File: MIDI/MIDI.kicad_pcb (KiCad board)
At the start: 2 copper layers, 85.8 x 137 mm, 136 parts, among them J1 DIN_5, J2 DIN_5, J3 DIN_5, J4 CONN_01X06, J5 CONN_01X06, SW1 SW_PUSH, SW10 SW_PUSH, SW11 SW_PUSH, SW12 SW_PUSH, SW2 SW_PUSH, SW3 SW_PUSH, SW4 SW_PUSH, SW5 SW_PUSH, SW6 SW_PUSH, SW7 SW_PUSH, SW8 SW_PUSH, SW9 SW_PUSH, U1 6N138, U2 4050, U3 40106, U4 ENCODER_w_SWITCH, U5 ENCODER_w_SWITCH, U6 ENCODER_w_SWITCH

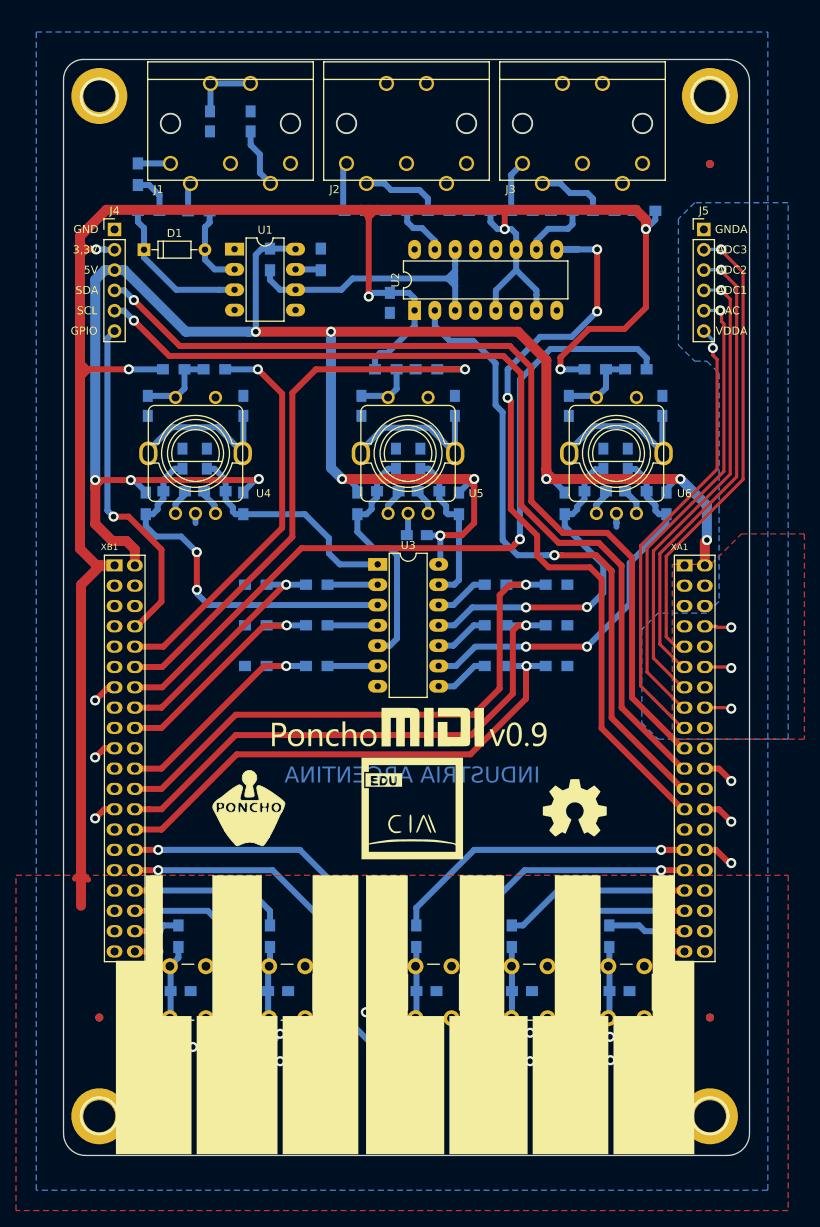
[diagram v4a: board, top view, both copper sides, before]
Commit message: Se finalizan los cambios según las revisiones
> Se realizan cambios segun detalles en archivos de revisiones.
> Se abandona requisito para asegurar fabricación artesanal por lo que se comienzan a utilizar los orificios metalizados para rutear.
> Se cambia la tensión de fijación de las compuertas no utilizadas en el 4050 para mejorar el plano de masa debajo del mismo.
> Se genera la versión 1.0 del diseño.
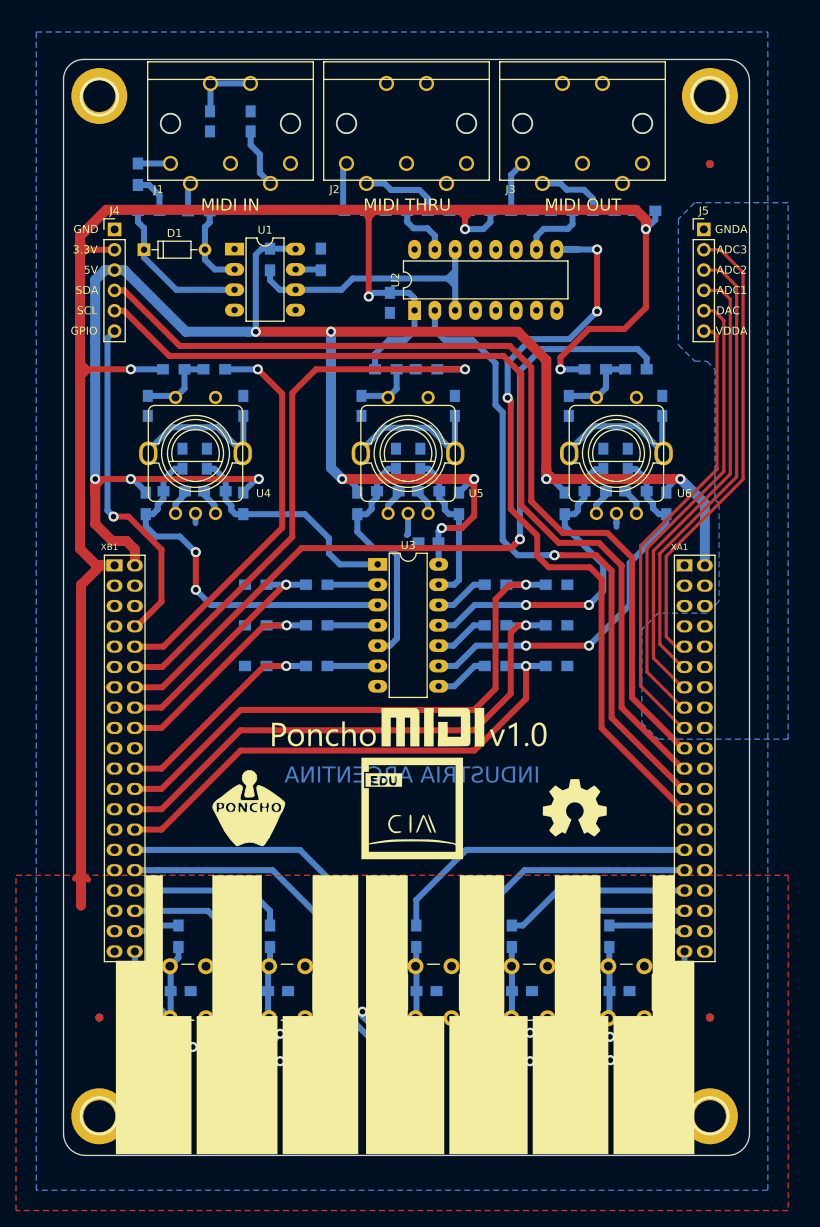
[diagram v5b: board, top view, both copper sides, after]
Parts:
- moved C16 1.72 mm to (87.1, 86.1)
- moved R39 0.51 mm to (52.1, 145.3)
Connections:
- U2 pad 11: +3.3V -> GND
- U2 pad 5: +3.3V -> GND
- U2 pad 7: +3.3V -> GND
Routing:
- net GND: track 26.2 -> 7.13 mm, vias 6 -> 0
- net +3.3V: track 318.9 -> 306.9 mm, vias 14 -> 13
- net GNDA: track 10.1 -> 0.00 mm, vias 3 -> 0
- net /Conectores/PUL0: track 21.1 -> 14.6 mm, vias 1 -> 0
- net /Conectores/PUL11: track 17.9 -> 14.7 mm, vias 1 -> 0
- net +5V: track 252.7 -> 251.1 mm, vias 11 -> 10
- net /Conectores/ENC_SW2: track 95.1 -> 95.7 mm
- net /Conectores/VDDA: track 56.7 -> 57.3 mm, vias 1 -> 0
- net /Conectores/PUL6: track 38.7 -> 39.3 mm, vias 1 -> 0
- net Net-(C18-Pad1): track 13.3 -> 12.8 mm
- net /Interfaz MIDI/TX-UART: track 97.0 -> 97.5 mm
- net /Conectores/PUL4: track 43.9 -> 43.4 mm, vias 1 -> 0
- net /Conectores/DAC: track 58.0 -> 57.5 mm, vias 1 -> 0
- net /Conectores/PUL5: track 50.6 -> 50.2 mm, vias 1 -> 0
- net /Conectores/ADC1: track 58.0 -> 58.1 mm, vias 1 -> 0
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- removed copper zone on F.Cu, net GNDA
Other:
- board text added: "MIDI IN"
- board text added: "MIDI OUT"
- board text added: "MIDI THRU"
